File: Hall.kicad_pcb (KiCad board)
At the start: 2 copper layers, 62 x 45.2 mm, 5 parts, among them J1 Conn_01x03_Pin

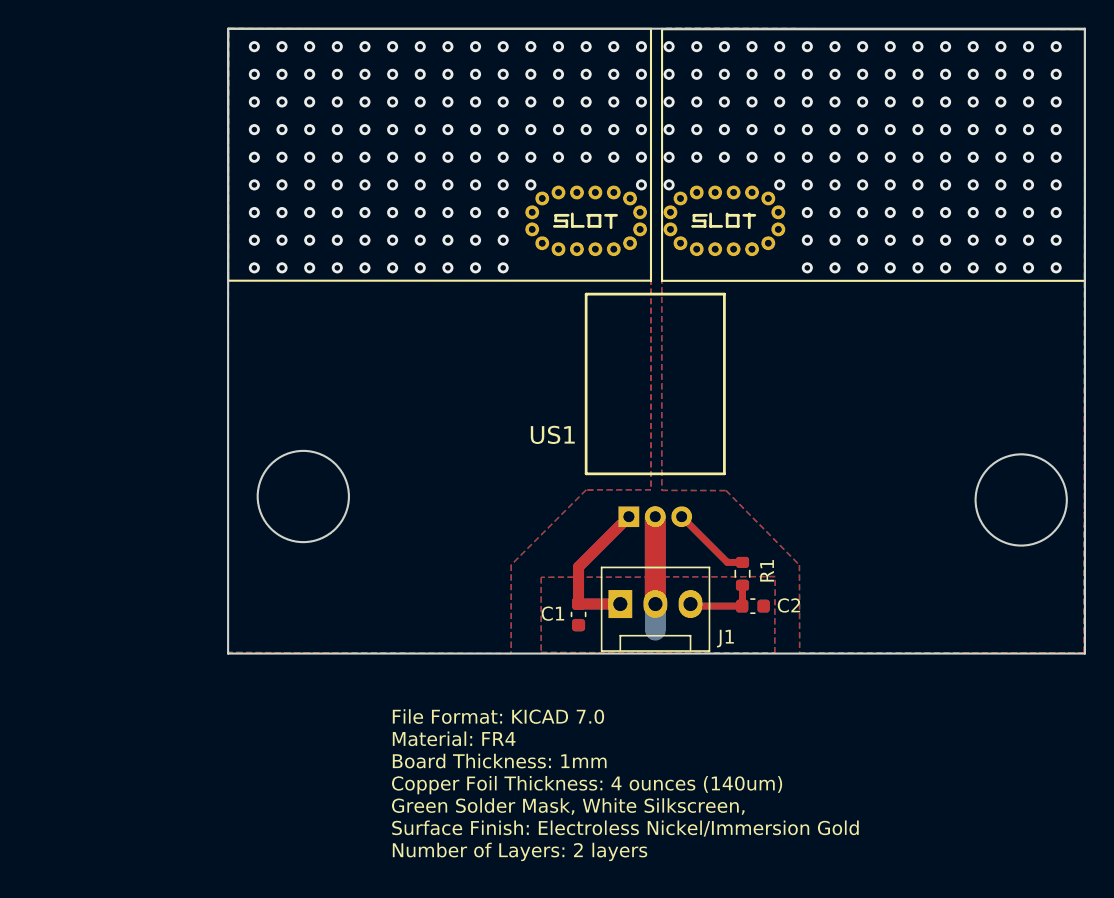
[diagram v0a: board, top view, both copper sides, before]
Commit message: Add files via upload
Add a voltage divider resistor for AD detection to enable the external 3.3V MCU to directly read the AD value.
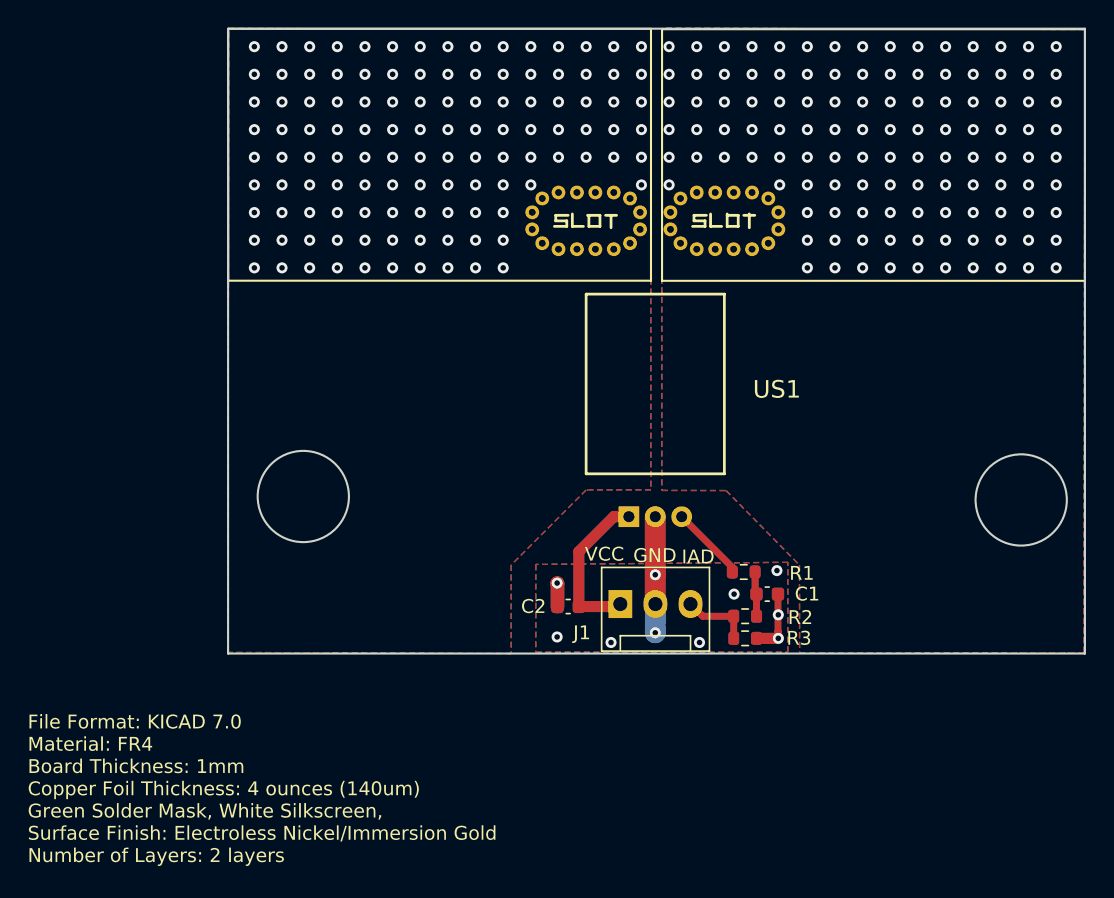
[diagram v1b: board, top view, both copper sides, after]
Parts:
- added R2: 300K, Resistor_SMD:R_0603_1608Metric, F.Cu at (120.6, 105.5)
- added R3: 100K, Resistor_SMD:R_0603_1608Metric, F.Cu at (120.6, 107.1)
- C1: value 0.1uF -> CF
- C2: value CF -> 0.1uF
- moved C1 13.7 mm to (122.2, 103.9), turned to 0 degrees
- moved C2 13.4 mm to (107.8, 104.8)
- moved R1 0.16 mm to (120.5, 102.3), turned to 180 degrees
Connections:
- C1 pad 1: GND1 -> /Vout
- C1 pad 2: VCC -> GND1
- C2 pad 1: /Vout -> GND1
- C2 pad 2: GND1 -> VCC
- J1 pad 3: /Vout -> /IAD
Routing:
- net GND1: track 14.6 -> 21.5 mm, vias 0 -> 10
- net /IAD: track 0.00 -> 5.09 mm
- net /Vout: track 5.22 -> 3.24 mm
- net VCC: track 10.8 -> 11.7 mm
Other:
- board text added: "GND"
- board text added: "IAD"
- board text added: "VCC"
